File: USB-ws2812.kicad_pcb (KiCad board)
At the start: 2 copper layers, 12 x 31.5 mm, 15 parts, among them J1 USB, J2 NEO_OUT, J3 GPIO, U1 ATTINY85-20PU, U2 WS2812B

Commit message: POWER CONNECTOR
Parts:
- removed M1: , Misc_Footprints:KEYCHAIN
- added ?: PWR, Pin_Headers:Pin_Header_Straight_1x02_Pitch2.54mm, F.Cu at (16.5, 16.0)
- J2: value NEO_OUT -> NEO
- moved U2 2.00 mm to (23.0, 17.5)
- moved J2 1.96 mm to (20.4, 16.5)
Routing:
- net GND: track 11.0 -> 31.1 mm, vias 3 -> 10
- net +5V: track 51.4 -> 64.7 mm, vias 4 -> 10
- net /NEO_I: track 3.44 -> 2.64 mm

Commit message: Fix careless mistakes (ZzZZZZzzzzz)
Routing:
- added copper zone on F.Cu, net +5V
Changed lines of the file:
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@@
     )
     (fp_line (start 2 -5.08) (end 2.5 -5.08) (layer B.SilkS) (width 0.15))
-    (fp_line (start 2 -2.5) (end 2.5 -2.5) (layer B.SilkS) (width 0.15))
-    (fp_line (start 2.25 -2.25) (end 2.25 -2.75) (layer B.SilkS) (width 0.15))
+    (fp_line (start 2 0) (end 2.5 0) (layer B.SilkS) (width 0.15))
+    (fp_line (start 2.25 0.25) (end 2.25 -0.25) (layer B.SilkS) (width 0.15))
     (fp_line (start -1.5 -6.25) (end 0.5 -6.25) (layer B.SilkS) (width 0.15))
     (fp_line (start -1.5 1.25) (end 0.5 1.25) (layer B.SilkS) (width 0.15))
@@
     (fp_line (start -1.5 1.25) (end -1.25 1.5) (layer B.SilkS) (width 0.15))
     (fp_line (start -1.5 1.25) (end -1.25 1) (layer B.SilkS) (width 0.15))
-    (fp_text user DO (at 2.25 -0.08 270) (layer B.SilkS)
+    (fp_text user DO (at 2.25 -2.5 270) (layer B.SilkS)
       (effects (font (size 0.5 0.5) (thickness 0.125)) (justify mirror))
     )
@@
   (gr_line (start 15 46) (end 15 14.5) (layer Edge.Cuts) (width 0.15))
   (gr_line (start 27 46) (end 27 14.5) (layer Edge.Cuts) (width 0.15))
+  (segment (start 25.75 35) (end 25.75 36) (width 1) (layer B.Cu) (net 1))
+  (segment (start 25.75 36) (end 24.81 36) (width 1) (layer B.Cu) (net 1))
+  (segment (start 24.8 35) (end 24.8 35.99) (width 1) (layer B.Cu) (net 1))
+  (segment (start 24.8 35.99) (end 24.81 36) (width 1) (layer B.Cu) (net 1))
+  (segment (start 24.8 35) (end 24.8 34) (width 1) (layer B.Cu) (net 1))
+  (segment (start 25.75 35) (end 24.8 35) (width 1) (layer B.Cu) (net 1))
+  (segment (start 25.75 34) (end 25.75 35) (width 1) (layer B.Cu) (net 1))
+  (segment (start 24.8 34) (end 25.75 34) (width 1) (layer B.Cu) (net 1))
   (segment (start 22.25 22.29999) (end 22.25 21) (width 1) (layer B.Cu) (net 1))
   (segment (start 22.25 27.94) (end 22.25 23.5) (width 1) (layer B.Cu) (net 1))
@@
   (segment (start 22.25 22.4) (end 22.25 21) (width 1) (layer B.Cu) (net 1))
   (segment (start 22.25 22.5) (end 22.25 22.4) (width 1) (layer B.Cu) (net 1))
-  (segment (start 25.75 36) (end 25.75 35) (width 1) (layer F.Cu) (net 1))
-  (segment (start 24.81 36) (end 25.75 36) (width 1) (layer F.Cu) (net 1))
-  (segment (start 24.8 35) (end 24.8 35.99) (width 1) (layer F.Cu) (net 1))
-  (segment (start 24.8 35.99) (end 24.81 36) (width 1) (layer F.Cu) (net 1))
-  (segment (start 24.8 35) (end 24.8 34) (width 1) (layer F.Cu) (net 1))
-  (segment (start 25.75 35) (end 24.8 35) (width 1) (layer F.Cu) (net 1))
-  (segment (start 25.75 34) (end 25.75 35) (width 1) (layer F.Cu) (net 1))
-  (segment (start 24.8 34) (end 25.75 34) (width 1) (layer F.Cu) (net 1))
   (via (at 25.75 36) (size 0.8) (drill 0.6) (layers F.Cu B.Cu) (net 1))
   (via (at 25.75 35) (size 0.8) (drill 0.6) (layers F.Cu B.Cu) (net 1))
@@
       )
     )
+  )
+  (zone (net 1) (net_name +5V) (layer F.Cu) (hatch edge 0.508)
+    (connect_pads (clearance 0.4))
+    (min_thickness 0.254)
+    (fill yes (arc_segments 16) (thermal_gap 0.508) (thermal_bridge_width 0.508))
+    (polygon
+      (pts
+        (xy 26.25 33.5) (xy 24.25 33.5) (xy 24.5 36.5) (xy 26.25 36.5)
+      )
+    )

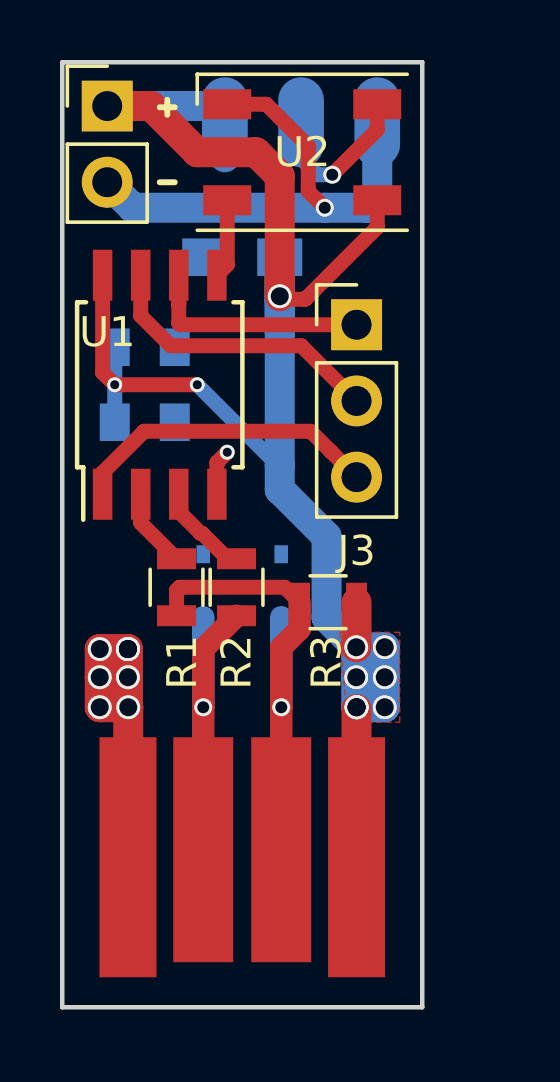
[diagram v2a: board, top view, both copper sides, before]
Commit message: New, smaller design
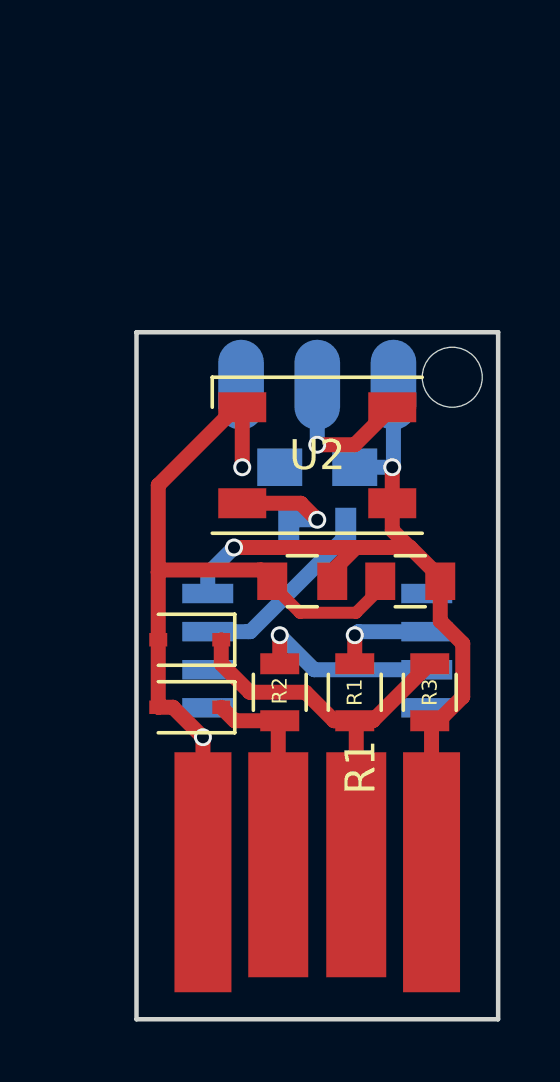
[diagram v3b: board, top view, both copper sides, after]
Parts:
- removed the ? at (16.5, 16.0)
- removed J3: GPIO, Pin_Headers:Pin_Header_Straight_1x03_Pitch2.54mm
- added ?: , Misc_Footprints:KEYCHAIN, F.Cu at (28.0, 25.0)
- added R4: R, Resistors_SMD:R_0805, B.Cu at (23.5, 30.0)
- C1, C2, D1, D2: moved to F.Cu
- U1: moved to B.Cu
- moved G*** 14.6 mm to (27.9, 44.0), turned to 180 degrees
- moved C1 10.3 mm to (26.6, 31.8), turned to 180 degrees
- moved U1 10.3 mm to (23.5, 34.1), turned to 180 degrees
- moved U2 10.1 mm to (23.5, 27.6)
- moved C2 9.40 mm to (23.0, 31.8), turned to 180 degrees
- moved J2 8.77 mm to (21.0, 25.2)
- moved C3 7.43 mm to (23.5, 28.0)
- moved R1 6.89 mm to (24.8, 35.5)
- moved R3 4.53 mm to (27.2, 35.5), turned to 90 degrees
- moved D2 4.07 mm to (19.2, 36.0), turned to 180 degrees
- moved R2 3.78 mm to (22.2, 35.5)
- moved D1 3.54 mm to (19.2, 33.8), turned to 180 degrees
- moved J1 2.55 mm to (23.5, 46.4)
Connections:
- net Net-(D1-Pad1) renamed /D-
- net Net-(D2-Pad1) renamed /D+
- net Net-(R1-Pad1) renamed /I_D-
- net Net-(R2-Pad1) renamed /I_D+
- J2 pad 1: +5V -> GND
- J2 pad 3: GND -> +5V
- U1 pad 1: /PB5 -> Net-(U1-Pad1)
- U1 pad 5: /NEO_I -> /PB0
- U1 pad 7: /PB4 -> /PB2
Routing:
- net +5V: track 64.7 -> 28.4 mm, vias 10 -> 2
- net /PB5: track 10.4 -> 0.00 mm
- net /PB4: track 9.72 -> 0.00 mm
- net /PB1: track 8.01 -> 0.00 mm
- net /PB2: track 0.00 -> 6.22 mm
- net /D+: track 11.3 -> 6.96 mm, vias 1 -> 0
- net /I_D+: track 3.39 -> 6.33 mm, vias 0 -> 1
- net GND: track 31.1 -> 28.5 mm, vias 10 -> 2
- net /D-: track 16.7 -> 14.4 mm, vias 1 -> 0
- net /NEO_I: track 2.64 -> 3.82 mm, vias 0 -> 1
- net /I_D-: track 2.64 -> 3.40 mm, vias 0 -> 1
- removed copper zone on F.Cu, net +5V
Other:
- board size 12 x 31.5 mm -> 12.1 x 22.9 mm
